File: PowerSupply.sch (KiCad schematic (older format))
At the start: 30 parts, among them J11 USB_B_Micro, J4 USB_B_Micro, J7 USB_B_Micro, J9 USB_B_Micro, U1 LPC54616J512, U11 MP1582EN-LF-Z, U6 TLV70233_SOT23-5

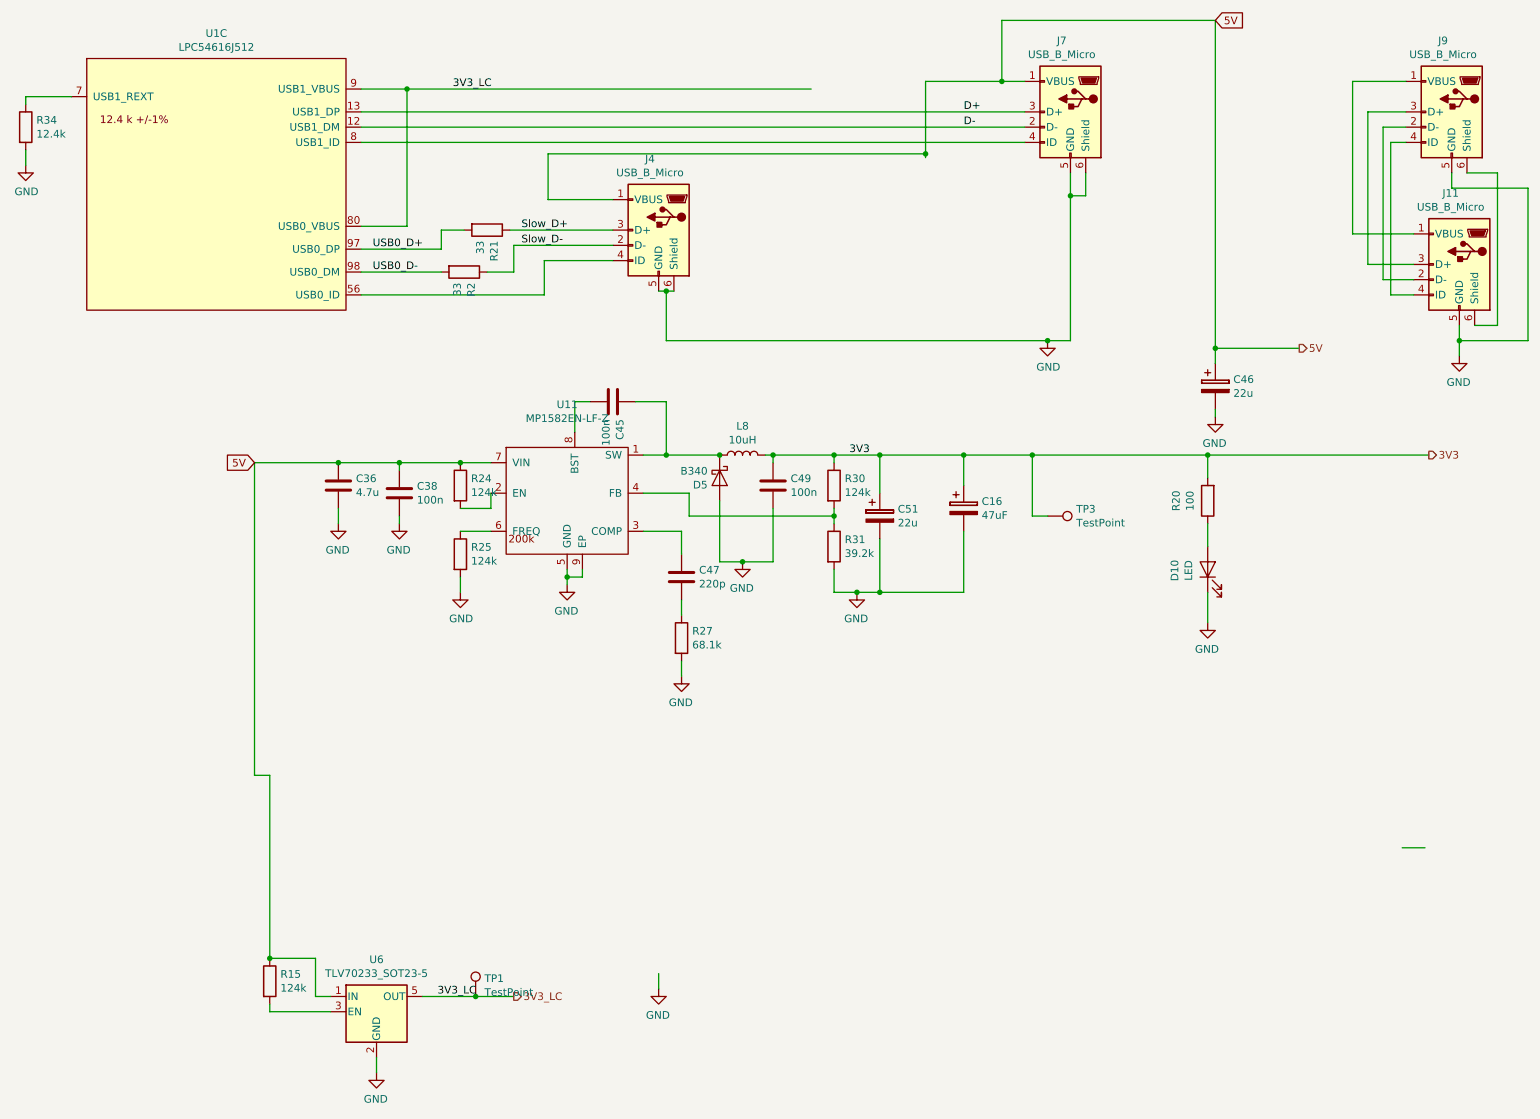
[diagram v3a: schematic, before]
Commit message: Switch to 4 Layer PCB as the RMII loopback doesn't work
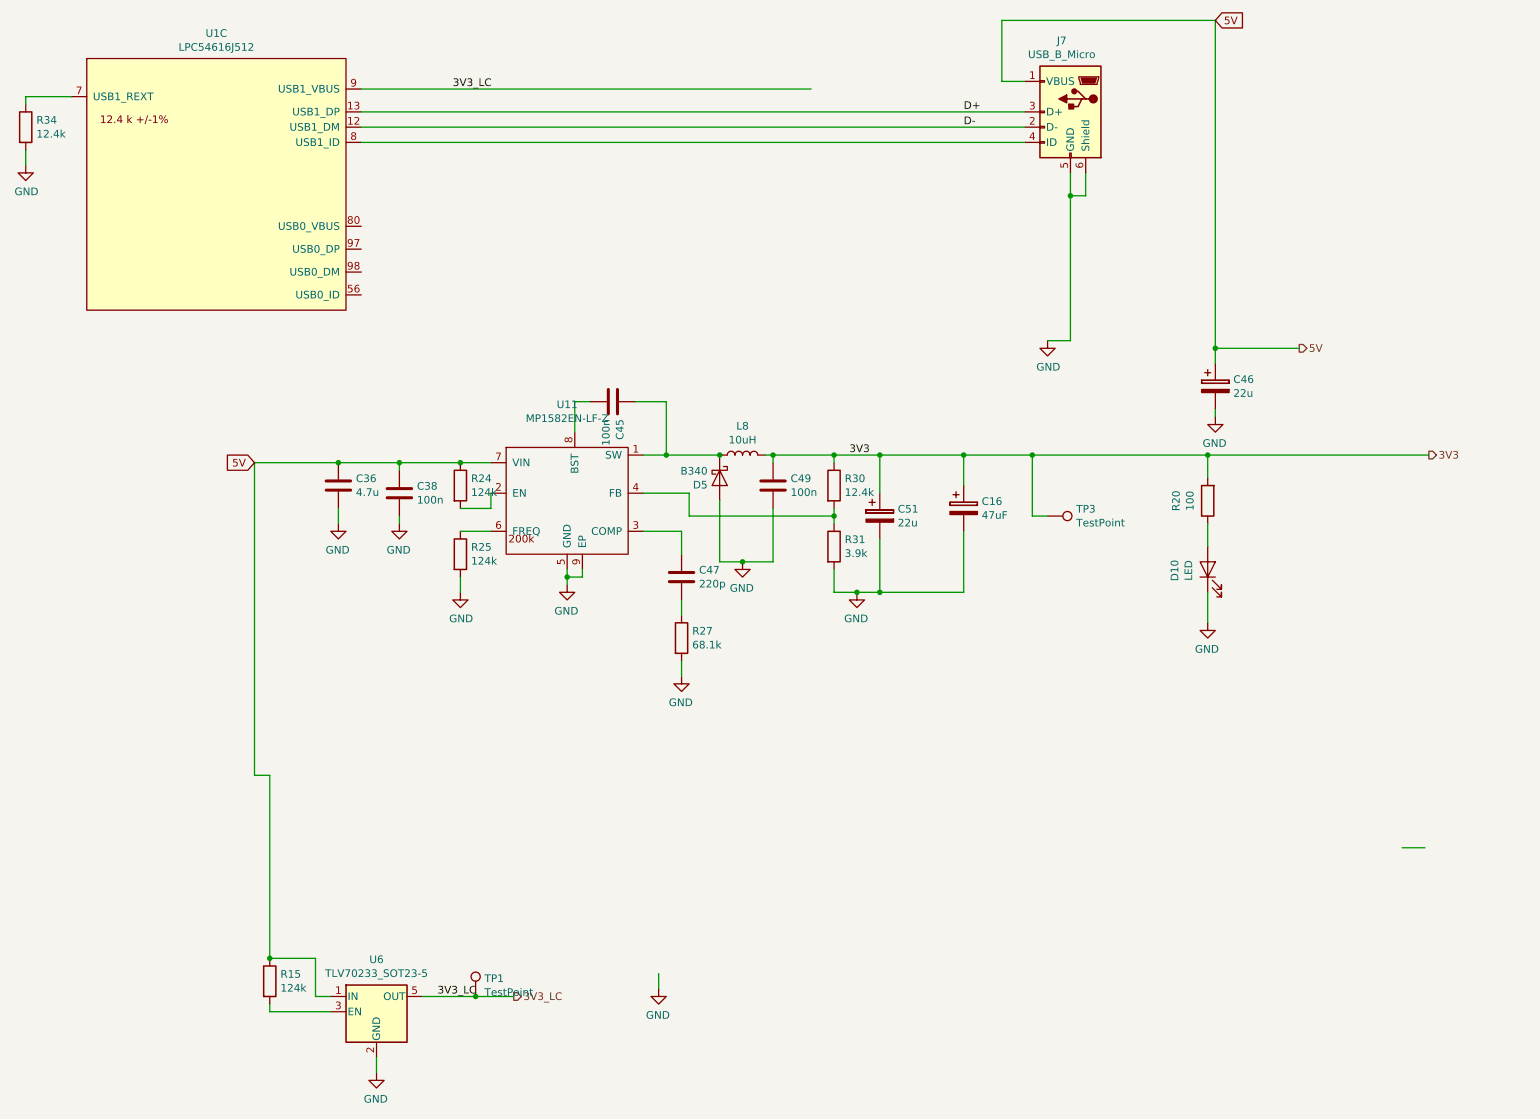
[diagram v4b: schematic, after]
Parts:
- removed J11, J4, J9: USB_B_Micro, cypress:MicroUsb, symbol canbox-rescue:USB_B_Micro-Connector
- removed R2, R21: 33, Resistor_SMD:R_0805_2012Metric_Pad1.15x1.40mm_HandSolder, symbol canbox-rescue:R-Device
- R30: value 124k -> 12.4k
- R31: value 39.2k -> 3.9k
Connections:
- net labels removed: Slow_D+, Slow_D-, USB0_D+, USB0_D-
- wire segments 133 -> 88
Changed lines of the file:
@@
 P 6400 3650
 F 0 "R30" H 6470 3696 50  0000 L CNN
-F 1 "124k" H 6470 3605 50  0000 L CNN
+F 1 "12.4k" H 6470 3605 50  0000 L CNN
 F 2 "Resistor_SMD:R_0805_2012Metric_Pad1.15x1.40mm_HandSolder" V 6330 3650 50  0001 C CNN
 F 3 "~" H 6400 3650 50  0001 C CNN
@@
 P 6400 4050
 F 0 "R31" H 6470 4096 50  0000 L CNN
-F 1 "39.2k" H 6470 4005 50  0000 L CNN
+F 1 "3.9k" H 6470 4005 50  0000 L CNN
 F 2 "Resistor_SMD:R_0805_2012Metric_Pad1.15x1.40mm_HandSolder" V 6330 4050 50  0001 C CNN
 F 3 "~" H 6400 4050 50  0001 C CNN
@@
 Wire Wire Line
 	8900 2750 9450 2750
-Connection ~ 7500 1000
-Wire Wire Line
-	7500 1000 7000 1000
 $Comp
 L canbox-rescue:CP-Device C46
@@
 	1    0    0    -1
 $EndComp
-Connection ~ 7800 2700
 Wire Wire Line
 	7800 2700 7950 2700
@@
 Wire Wire Line
 	3300 1200 7650 1200
-$Comp
-L canbox-rescue:USB_B_Micro-Connector J4
-U 1 1 5F413967
-P 5250 1975
-F 0 "J4" H 5307 2442 50  0000 C CNN
-F 1 "USB_B_Micro" H 5307 2351 50  0000 C CNN
-F 2 "cypress:MicroUsb" H 5400 1925 50  0001 C CNN
-F 3 "~" H 5400 1925 50  0001 C CNN
-F 4 "1050170001" H 5250 1975 50  0001 C CNN "OP"
-F 5 "ali" H -2700 775 50  0001 C CNN "notes"
-	1    5250 1975
-	-1   0    0    -1
-$EndComp
-Wire Wire Line
-	3825 1975 3825 2100
-Wire Wire Line
-	3825 2100 3300 2100
-Wire Wire Line
-	3300 2250 3825 2250
-Wire Wire Line
-	5250 2375 5300 2375
-Connection ~ 5300 2375
-Wire Wire Line
-	5300 2375 5350 2375
-Wire Wire Line
-	3300 1050 3600 1050
-Wire Wire Line
-	4525 1475 4525 1775
-Wire Wire Line
-	5300 2375 5300 2700
-Wire Wire Line
-	3600 1950 3300 1950
-Wire Wire Line
-	4525 1775 4950 1775
-Wire Wire Line
-	3600 1950 3600 1050
-Connection ~ 3600 1050
-Wire Wire Line
-	3600 1050 6250 1050
-Wire Wire Line
-	4950 2175 4500 2175
-Wire Wire Line
-	4500 2175 4500 2400
-Wire Wire Line
-	4500 2400 3300 2400
-Text Label 4350 1975 0    50   ~ 0
-Slow_D+
-Text Label 4350 2075 0    50   ~ 0
-Slow_D-
-$Comp
-L canbox-rescue:R-Device R21
-U 1 1 5F4C53F3
-P 4125 1975
-F 0 "R21" H 4195 2021 50  0000 L CNN
-F 1 "33" H 4195 1930 50  0000 L CNN
-F 2 "Resistor_SMD:R_0805_2012Metric_Pad1.15x1.40mm_HandSolder" V 4055 1975 50  0001 C CNN
-F 3 "~" H 4125 1975 50  0001 C CNN
-F 4 "0805W8F1243T5E" H -2275 -1675 50  0001 C CNN "OP"
-F 5 "ok" H -2875 -25 50  0001 C CNN "Mouser"
-F 6 "ok" H -2875 -25 50  0001 C CNN "notes"
-F 7 "C17440" H 4125 1975 50  0001 C CNN "JLC"
-	1    4125 1975
-	0    1    1    0
-$EndComp
-Wire Wire Line
-	3975 1975 3825 1975
-$Comp
-L canbox-rescue:R-Device R2
-U 1 1 5F4CBF14
-P 3975 2250
-F 0 "R2" H 4045 2296 50  0000 L CNN
-F 1 "33" H 4045 2205 50  0000 L CNN
-F 2 "Resistor_SMD:R_0805_2012Metric_Pad1.15x1.40mm_HandSolder" V 3905 2250 50  0001 C CNN
-F 3 "~" H 3975 2250 50  0001 C CNN
-F 4 "0805W8F1243T5E" H -2425 -1400 50  0001 C CNN "OP"
-F 5 "ok" H -3025 250 50  0001 C CNN "Mouser"
-F 6 "ok" H -3025 250 50  0001 C CNN "notes"
-F 7 "C17440" H 3975 2250 50  0001 C CNN "JLC"
-	1    3975 2250
-	0    1    1    0
-$EndComp
-Text Label 3375 2100 0    50   ~ 0
-USB0_D+
-Text Label 3375 2250 0    50   ~ 0
-USB0_D-
-Wire Wire Line
-	4125 2250 4300 2250
-Wire Wire Line
-	4300 2250 4300 2075
-Wire Wire Line
-	4300 2075 4950 2075
-Wire Wire Line
-	4950 1975 4275 1975
-Wire Wire Line
-	5300 2700 7800 2700
-Wire Wire Line
-	7000 1475 4525 1475
-Wire Wire Line
-	7000 1000 7000 1475
-Connection ~ 7000 1475
-Wire Wire Line
-	7000 1475 7000 1500
 Wire Wire Line
 	6000 3450 6400 3450
@@
 	-1   0    0    -1
 $EndComp
-$Comp
-L canbox-rescue:USB_B_Micro-Connector J9
-U 1 1 5E3C43EB
-P 10450 1200
-F 0 "J9" H 10507 1667 50  0000 C CNN
-F 1 "USB_B_Micro" H 10507 1576 50  0000 C CNN
-F 2 "cypress:MicroUsb" H 10600 1150 50  0001 C CNN
-F 3 "~" H 10600 1150 50  0001 C CNN
-F 4 "1050170001" H 10450 1200 50  0001 C CNN "OP"
-F 5 "ali" H 2500 0   50  0001 C CNN "notes"
-	1    10450 1200
-	-1   0    0    -1
-$EndComp
-$Comp
-L canbox-rescue:USB_B_Micro-Connector J11
-U 1 1 5E3D3C08
-P 10500 2200
-F 0 "J11" H 10557 2667 50  0000 C CNN
-F 1 "USB_B_Micro" H 10557 2576 50  0000 C CNN
-F 2 "cypress:MicroUsb" H 10650 2150 50  0001 C CNN
-F 3 "~" H 10650 2150 50  0001 C CNN
-F 4 "1050170001" H 10500 2200 50  0001 C CNN "OP"
-F 5 "ali" H 2550 1000 50  0001 C CNN "notes"
-	1    10500 2200
-	-1   0    0    -1
-$EndComp
-Wire Wire Line
-	10150 1000 9800 1000
-Wire Wire Line
-	9800 1000 9800 2000
-Wire Wire Line
-	9800 2000 10200 2000
-Wire Wire Line
-	10200 2200 9900 2200
-Wire Wire Line
-	9900 2200 9900 1200
-Wire Wire Line
-	9900 1200 10150 1200
-Wire Wire Line
-	10150 1300 10000 1300
-Wire Wire Line
-	10000 1300 10000 2300
-Wire Wire Line
-	10000 2300 10200 2300
-Wire Wire Line
-	10200 2400 10050 2400
-Wire Wire Line
-	10050 2400 10050 1400
-Wire Wire Line
-	10050 1400 10150 1400
-$Comp
-L canbox-rescue:GND-power #PWR0109
-U 1 1 5E3DA6CD
-P 10500 2800
-F 0 "#PWR0109" H 10500 2550 50  0001 C CNN
-F 1 "GND" H 10505 2627 50  0000 C CNN
-F 2 "" H 10500 2800 50  0001 C CNN
-F 3 "" H 10500 2800 50  0001 C CNN
-	1    10500 2800
-	-1   0    0    -1
-$EndComp
-Wire Wire Line
-	10500 2800 10500 2700
-Wire Wire Line
-	10950 2700 10950 1700
-Wire Wire Line
-	10950 1700 10450 1700
-Wire Wire Line
-	10450 1700 10450 1600
-Wire Wire Line
-	10500 2700 10950 2700
-Connection ~ 10500 2700
-Wire Wire Line
-	10500 2700 10500 2600
-Wire Wire Line
-	10550 1600 10750 1600
-Wire Wire Line
-	10750 1600 10750 2600
-Wire Wire Line
-	10750 2600 10600 2600
+Wire Wire Line
+	3300 1050 6250 1050
 $EndSCHEMATC

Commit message: V5 now impedance controlled
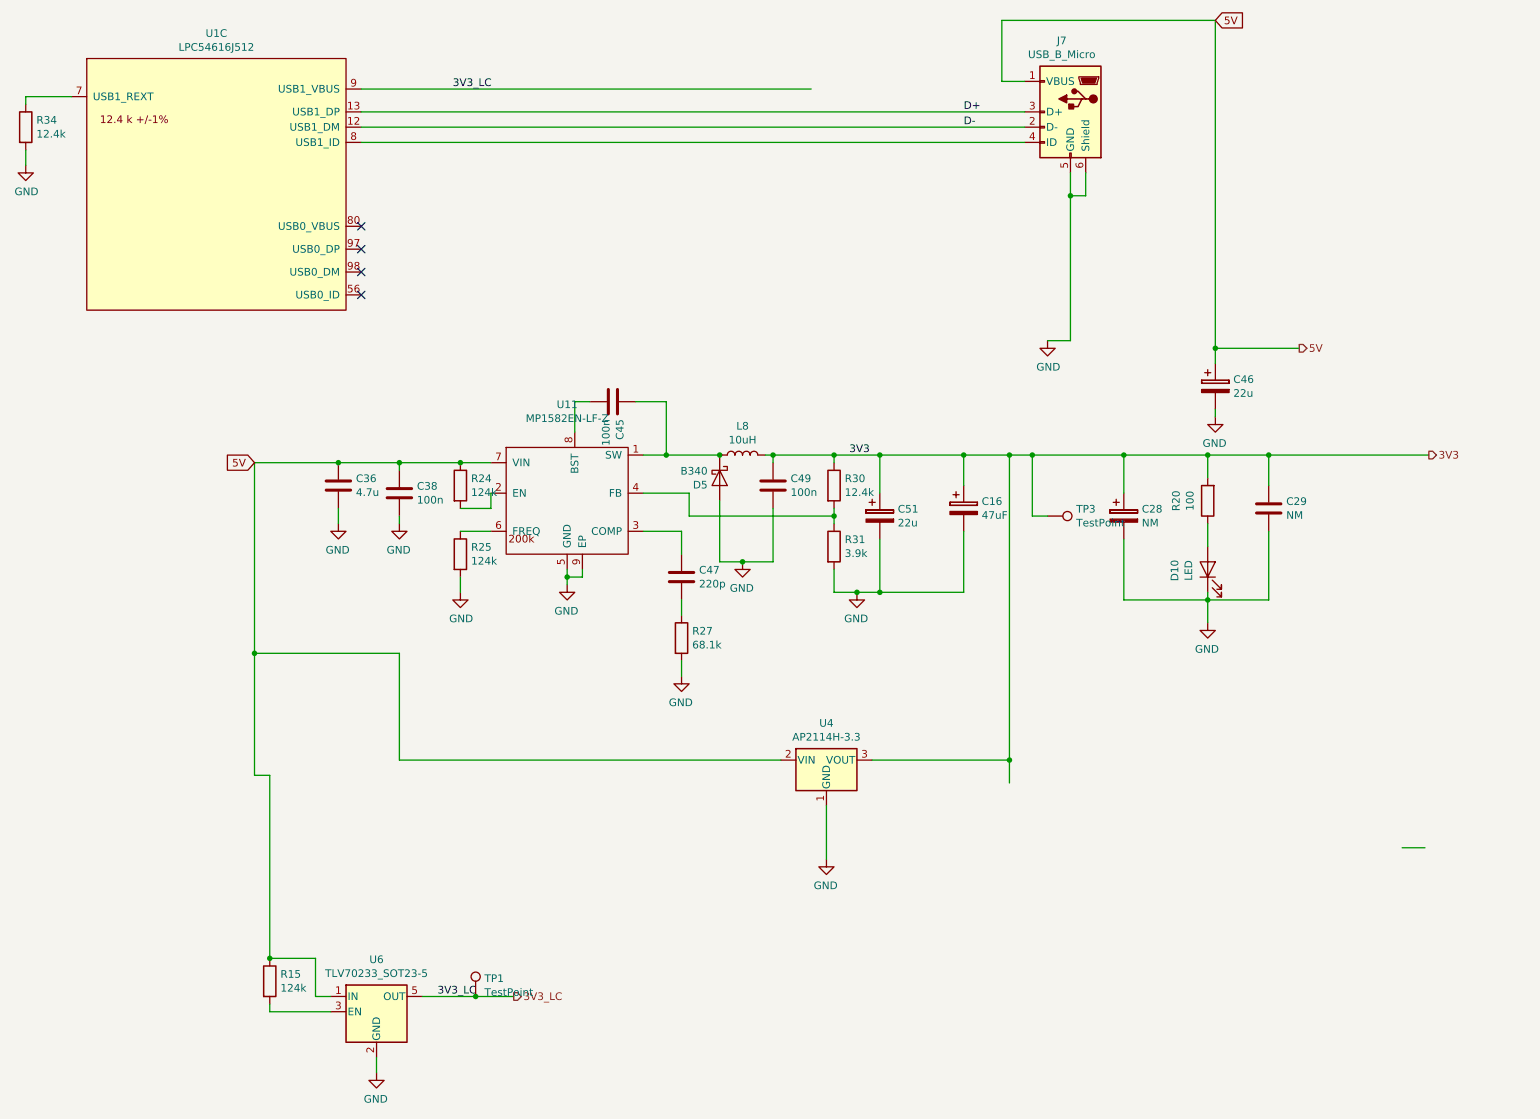
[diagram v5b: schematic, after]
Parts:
- added C28: NM, Capacitor_Tantalum_SMD:CP_EIA-3528-21_Kemet-B_Pad1.50x2.35mm_HandSolder, symbol canbox-rescue:CP-Device
- added C29: NM, Capacitor_SMD:C_0805_2012Metric_Pad1.15x1.40mm_HandSolder, symbol canbox-rescue:C-Device
- added U4: AP2114H-3.3, Package_TO_SOT_SMD:SOT-223-3_TabPin2, symbol cypress:AP2114H-3.3
- C51: footprint Capacitor_SMD:C_0805_2012Metric_Pad1.15x1.40mm_HandSolder -> Capacitor_Tantalum_SMD:CP_EIA-3528-21_Kemet-B_Pad1.50x2.35mm_HandSolder
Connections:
- wire segments 88 -> 105
- no-connect marks 0 -> 4
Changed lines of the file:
@@
 F 0 "C51" H 6818 3896 50  0000 L CNN
 F 1 "22u" H 6818 3805 50  0000 L CNN
-F 2 "Capacitor_SMD:C_0805_2012Metric_Pad1.15x1.40mm_HandSolder" H 6738 3700 50  0001 C CNN
+F 2 "Capacitor_Tantalum_SMD:CP_EIA-3528-21_Kemet-B_Pad1.50x2.35mm_HandSolder" H 6738 3700 50  0001 C CNN
 F 3 "~" H 6700 3850 50  0001 C CNN
 F 4 "C0805C224Z3VACTU" H 0   0   50  0001 C CNN "OP"
@@
 Connection ~ 7700 3450
 Wire Wire Line
-	7700 3450 8850 3450
+	7700 3450 8300 3450
 $Comp
 L canbox-rescue:TestPoint-Connector TP3
@@
 	2600 3500 3150 3500
 Wire Wire Line
-	5250 6950 5250 6850
-Wire Wire Line
 	4050 7000 4300 7000
 $Comp
@@
 $EndComp
 Wire Wire Line
-	2600 5550 2600 3500
+	2600 5550 2600 4750
 $Comp
 L canbox-rescue:GND-power #PWR041
 U 1 1 5C045BB1
-P 5250 6950
-F 0 "#PWR041" H 5250 6700 50  0001 C CNN
-F 1 "GND" H 5255 6777 50  0000 C CNN
-F 2 "" H 5250 6950 50  0001 C CNN
-F 3 "" H 5250 6950 50  0001 C CNN
-	1    5250 6950
+P 6350 6100
+F 0 "#PWR041" H 6350 5850 50  0001 C CNN
+F 1 "GND" H 6355 5927 50  0000 C CNN
+F 2 "" H 6350 6100 50  0001 C CNN
+F 3 "" H 6350 6100 50  0001 C CNN
+	1    6350 6100
 	-1   0    0    -1
 $EndComp
@@
 Connection ~ 7250 3450
 Wire Wire Line
-	7250 3450 7700 3450
+	7250 3450 7550 3450
 Wire Wire Line
 	6700 4350 7250 4350
@@
 Connection ~ 8850 3450
 Wire Wire Line
-	8850 3450 10300 3450
+	8850 3450 9250 3450
 $Comp
 L canbox-rescue:GND-power #PWR0107
@@
 	8850 3900 8850 4050
 Wire Wire Line
-	8850 4350 8850 4550
+	8850 4350 8850 4400
 Wire Wire Line
 	3300 1300 7650 1300
@@
 Wire Wire Line
 	3300 1050 6250 1050
+Wire Wire Line
+	7550 5450 7550 3450
+Connection ~ 7550 3450
+Wire Wire Line
+	7550 3450 7700 3450
+Wire Wire Line
+	7550 5600 7550 5450
+Connection ~ 7550 5450
+Wire Wire Line
+	3550 5450 3550 4750
+Wire Wire Line
+	3550 4750 2600 4750
+Connection ~ 2600 4750
+Wire Wire Line
+	2600 4750 2600 3500
+$Comp
+L cypress:AP2114H-3.3 U4
+U 1 1 5DF51146
+P 6350 5450
+F 0 "U4" H 6350 5692 50  0000 C CNN
+F 1 "AP2114H-3.3" H 6350 5601 50  0000 C CNN
+F 2 "Package_TO_SOT_SMD:SOT-223-3_TabPin2" H 6350 5675 50  0001 C CNN
+F 3 "https://www.diodes.com/assets/Datasheets/AP2204.pdf" H 6350 5450 50  0001 C CNN
+	1    6350 5450
+	1    0    0    -1
+$EndComp
+Wire Wire Line
+	6650 5450 7550 5450
+Wire Wire Line
+	6350 5750 6350 6100
+Wire Wire Line
+	3550 5450 6050 5450
+NoConn ~ 3300 1950
+NoConn ~ 3300 2100
+NoConn ~ 3300 2250
+NoConn ~ 3300 2400
+$Comp
+L canbox-rescue:CP-Device C28
+U 1 1 5EB127DA
+P 8300 3850
+F 0 "C28" H 8418 3896 50  0000 L CNN
+F 1 "NM" H 8418 3805 50  0000 L CNN
+F 2 "Capacitor_Tantalum_SMD:CP_EIA-3528-21_Kemet-B_Pad1.50x2.35mm_HandSolder" H 8338 3700 50  0001 C CNN
+F 3 "~" H 8300 3850 50  0001 C CNN
+F 4 "CL21A226MAQNNNE" H 1600 0   50  0001 C CNN "OP"
+F 5 "ali" H 1600 0   50  0001 C CNN "notes"
+F 6 "C45783 " H 8300 3850 50  0001 C CNN "JLC"
+	1    8300 3850
+	1    0    0    -1
+$EndComp
+Wire Wire Line
+	8300 3700 8300 3450
+Connection ~ 8300 3450
+Wire Wire Line
+	8300 3450 8850 3450
+Wire Wire Line
+	8300 4400 8300 4000
+Wire Wire Line
+	8300 4400 8850 4400
+Connection ~ 8850 4400
+Wire Wire Line
+	8850 4400 8850 4550
+$Comp
+L canbox-rescue:C-Device C29
+U 1 1 5EB1AE20
+P 9250 3800
+F 0 "C29" H 9365 3846 50  0000 L CNN
+F 1 "NM" H 9365 3755 50  0000 L CNN
+F 2 "Capacitor_SMD:C_0805_2012Metric_Pad1.15x1.40mm_HandSolder" H 9288 3650 50  0001 C CNN
+F 3 "~" H 9250 3800 50  0001 C CNN
+F 4 "CC0805KRX7R9BB104" H 3250 150 50  0001 C CNN "OP"
+F 5 "ali" H 5700 100 50  0001 C CNN "notes"
+F 6 " C49678 " H 9250 3800 50  0001 C CNN "JLC"
+	1    9250 3800
+	1    0    0    -1
+$EndComp
+Wire Wire Line
+	9250 3650 9250 3450
+Connection ~ 9250 3450
+Wire Wire Line
+	9250 3450 10300 3450
+Wire Wire Line
+	8850 4400 9250 4400
+Wire Wire Line
+	9250 4400 9250 3950
 $EndSCHEMATC
